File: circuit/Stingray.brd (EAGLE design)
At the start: 45.7 x 50.8 mm, 18 parts, among them IC1 4052N, IC2 4052N, K1 5200, K3 PN87520-S, M1 ARDUINO-NANO-3.0

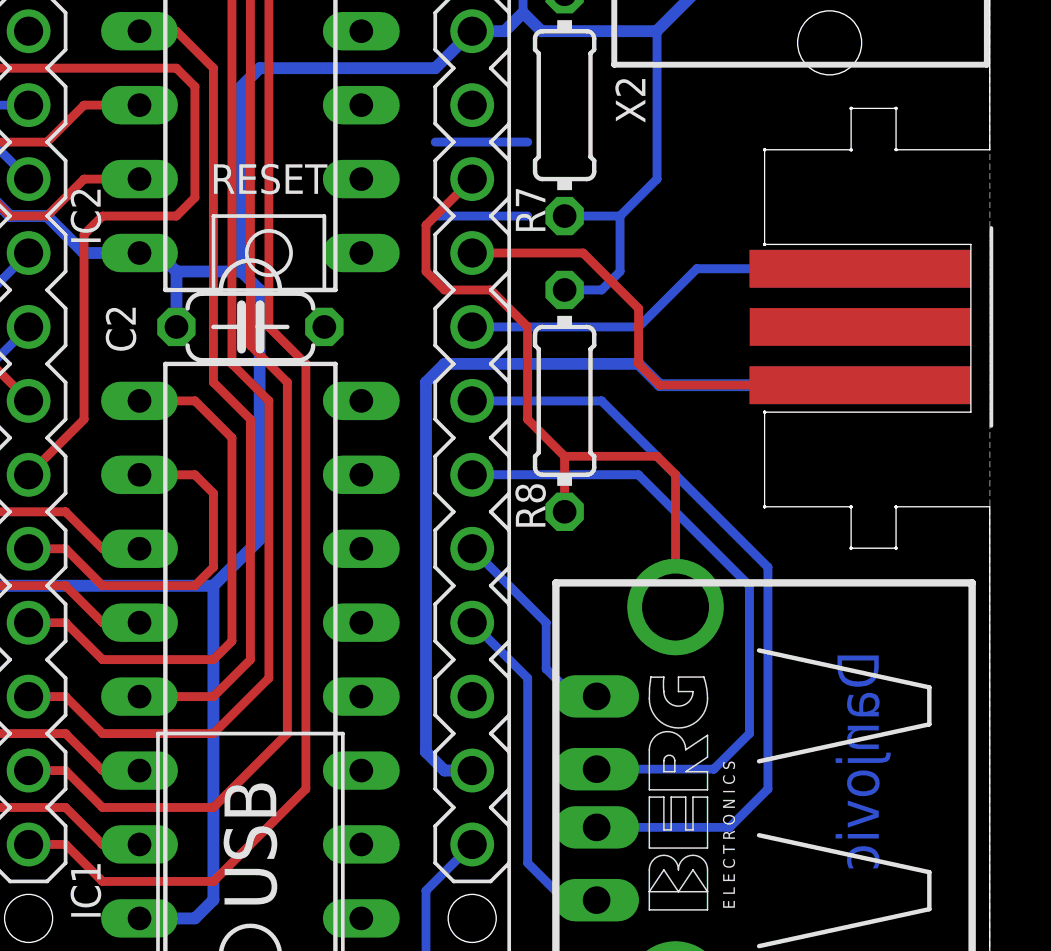
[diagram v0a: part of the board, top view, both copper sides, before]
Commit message: Corrected mirrored Wii connector footprint
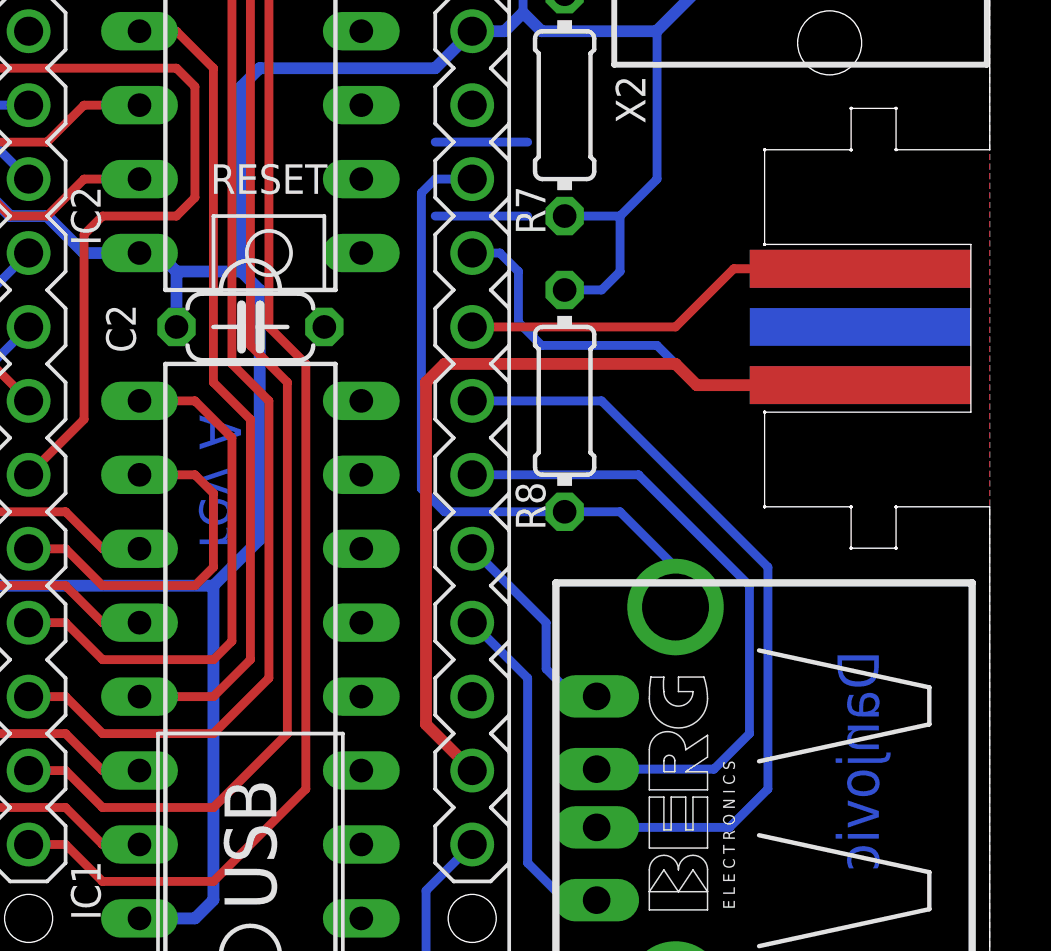
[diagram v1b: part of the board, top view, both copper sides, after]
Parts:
- flipped K2 to the bottom, turned to 180 degrees
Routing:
- net +3V3: track 30.0 -> 29.5 mm
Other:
- board text added: "rev A"

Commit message: Updated value of R1 to 1K
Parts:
- R1: value 4k7 -> 1k
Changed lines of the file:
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@@
 <?xml version="1.0" encoding="utf-8"?>
 <!DOCTYPE eagle SYSTEM "eagle.dtd">
-<eagle version="7.2.0">
+<eagle version="6.5.0">
 <drawing>
 <settings>
@@
 <pass name="Default">
 <param name="RoutingGrid" value="50mil"/>
-<param name="AutoGrid" value="1"/>
-<param name="Efforts" value="0"/>
-<param name="TopRouterVariant" value="1"/>
 <param name="tpViaShape" value="round"/>
-<param name="PrefDir.1" value="a"/>
+<param name="PrefDir.1" value="|"/>
 <param name="PrefDir.2" value="0"/>
 <param name="PrefDir.3" value="0"/>
@@
 <param name="PrefDir.14" value="0"/>
 <param name="PrefDir.15" value="0"/>
-<param name="PrefDir.16" value="a"/>
+<param name="PrefDir.16" value="-"/>
 <param name="cfVia" value="8"/>
 <param name="cfNonPref" value="5"/>
@@
 <attribute name="VALUE" x="20.955" y="45.085" size="1.016" layer="27" rot="R180" align="top-center"/>
 </element>
-<element name="R1" library="rcl" package="0204/7" value="4k7" x="7.62" y="6.35" smashed="yes" rot="R90">
+<element name="R1" library="rcl" package="0204/7" value="1k" x="7.62" y="6.35" smashed="yes" rot="R90">
 <attribute name="NAME" x="6.3246" y="1.905" size="1.016" layer="25" ratio="10" rot="R90"/>
 <attribute name="VALUE" x="8.1026" y="5.3594" size="0.9906" layer="27" ratio="10" rot="R90"/>
